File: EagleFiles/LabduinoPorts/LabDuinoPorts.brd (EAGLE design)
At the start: 56.8 x 16.5 mm, 22 parts

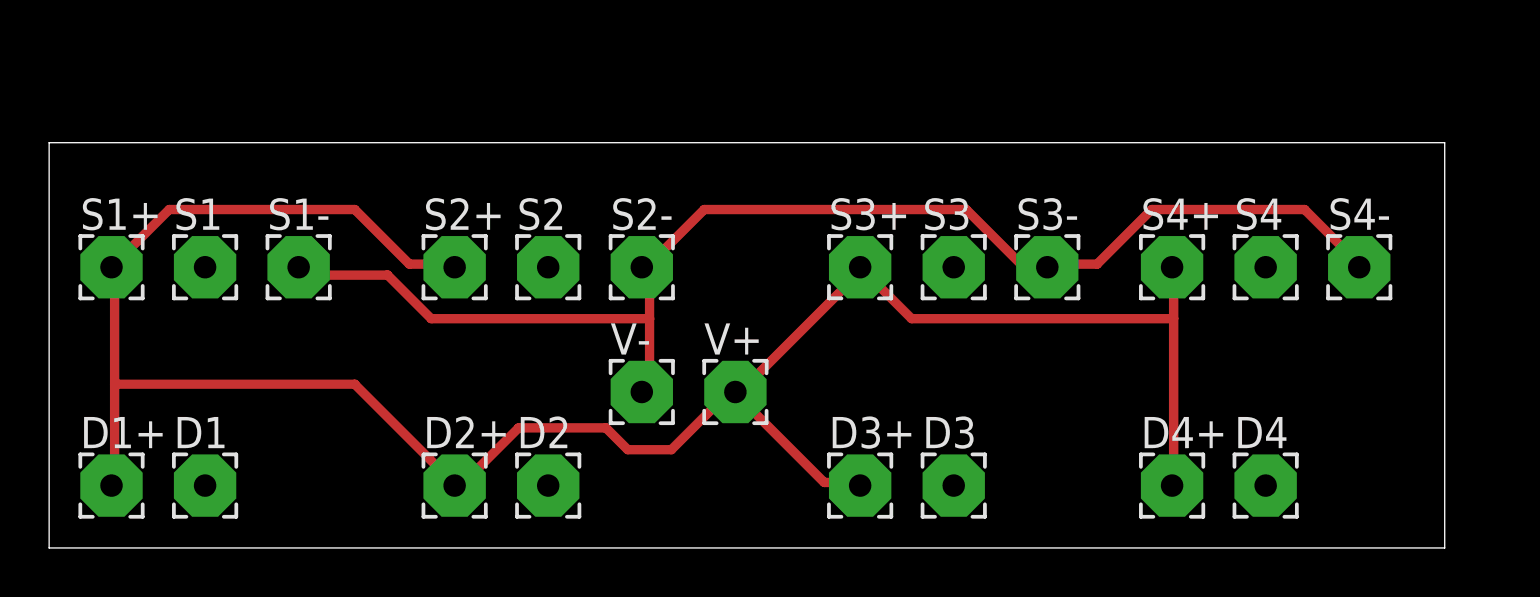
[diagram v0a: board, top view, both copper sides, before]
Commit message: Eagle LabDuinoPorts Update
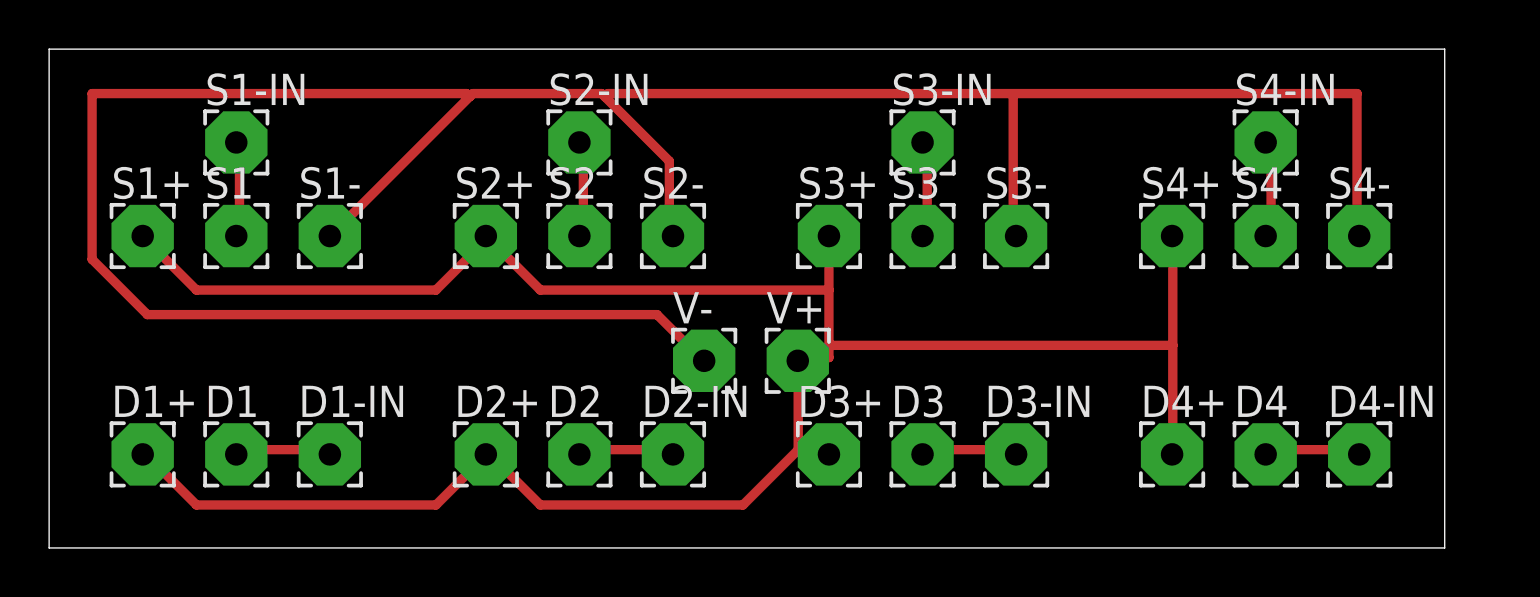
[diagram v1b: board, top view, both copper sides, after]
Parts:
- added D1-IN, D2-IN, D3-IN, D4-IN, S1-IN, S2-IN, S3-IN, S4-IN: (no value), wirepad:2,54/0,9
- moved V- 2.84 mm to (26.7, 7.62)
- moved V+ 2.84 mm to (30.5, 7.62)
- moved D3+ 1.80 mm to (31.8, 3.81)
- moved S3+ 1.80 mm to (31.8, 12.7)
- moved S3- 1.80 mm to (39.4, 12.7)
- moved D1 1.80 mm to (7.62, 3.81)
- moved D1+ 1.80 mm to (3.81, 3.81)
- moved D2 1.80 mm to (21.6, 3.81)
- moved D2+ 1.80 mm to (17.8, 3.81)
- moved S1 1.80 mm to (7.62, 12.7)
- moved S1+ 1.80 mm to (3.81, 12.7)
- moved S1- 1.80 mm to (11.4, 12.7)
- moved S2 1.80 mm to (21.6, 12.7)
- moved S2+ 1.80 mm to (17.8, 12.7)
- moved S2- 1.80 mm to (25.4, 12.7)
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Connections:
- new net N$1: S1-IN.1, S1.1
- new net N$2: S2-IN.1, S2.1
- new net N$3: S3-IN.1, S3.1
- new net N$4: S4-IN.1, S4.1
- new net N$5: D1-IN.1, D1.1
- new net N$6: D2-IN.1, D2.1
- new net N$7: D3-IN.1, D3.1
- new net N$8: D4-IN.1, D4.1
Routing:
- net GND: track 53.7 -> 111.7 mm
- net VCC: track 90.7 -> 96.5 mm
- net N$4: track 0.00 -> 4.20 mm
- net N$3: track 0.00 -> 4.14 mm
- net N$2: track 0.00 -> 4.08 mm
- net N$1: track 0.00 -> 4.02 mm
- net N$8: track 0.00 -> 4.00 mm
- net N$7: track 0.00 -> 3.99 mm
- net N$5: track 0.00 -> 3.99 mm
- net N$6: track 0.00 -> 3.99 mm
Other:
- board size 56.8 x 16.5 mm -> 56.8 x 20.3 mm
